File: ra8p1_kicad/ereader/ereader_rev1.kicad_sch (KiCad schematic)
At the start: 1 part, among them U1 R7KA8P1KFLCAC#UC0

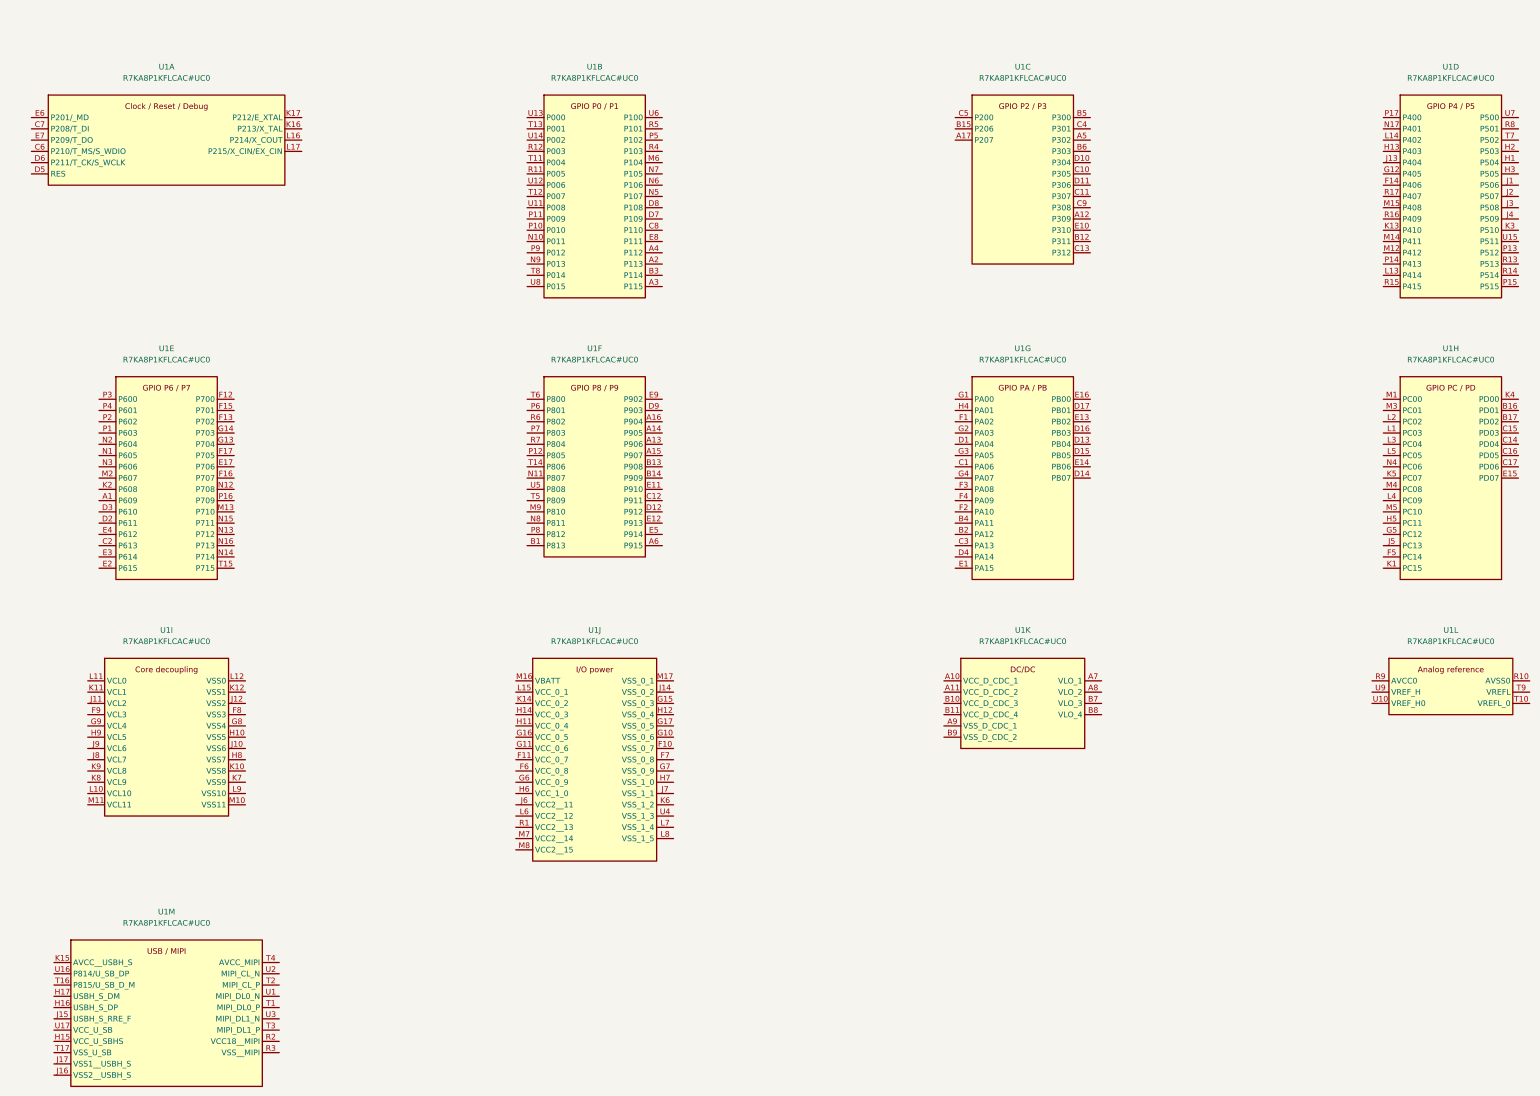
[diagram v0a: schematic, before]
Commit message: feat(hardware): split processor sheets and wire core power draft
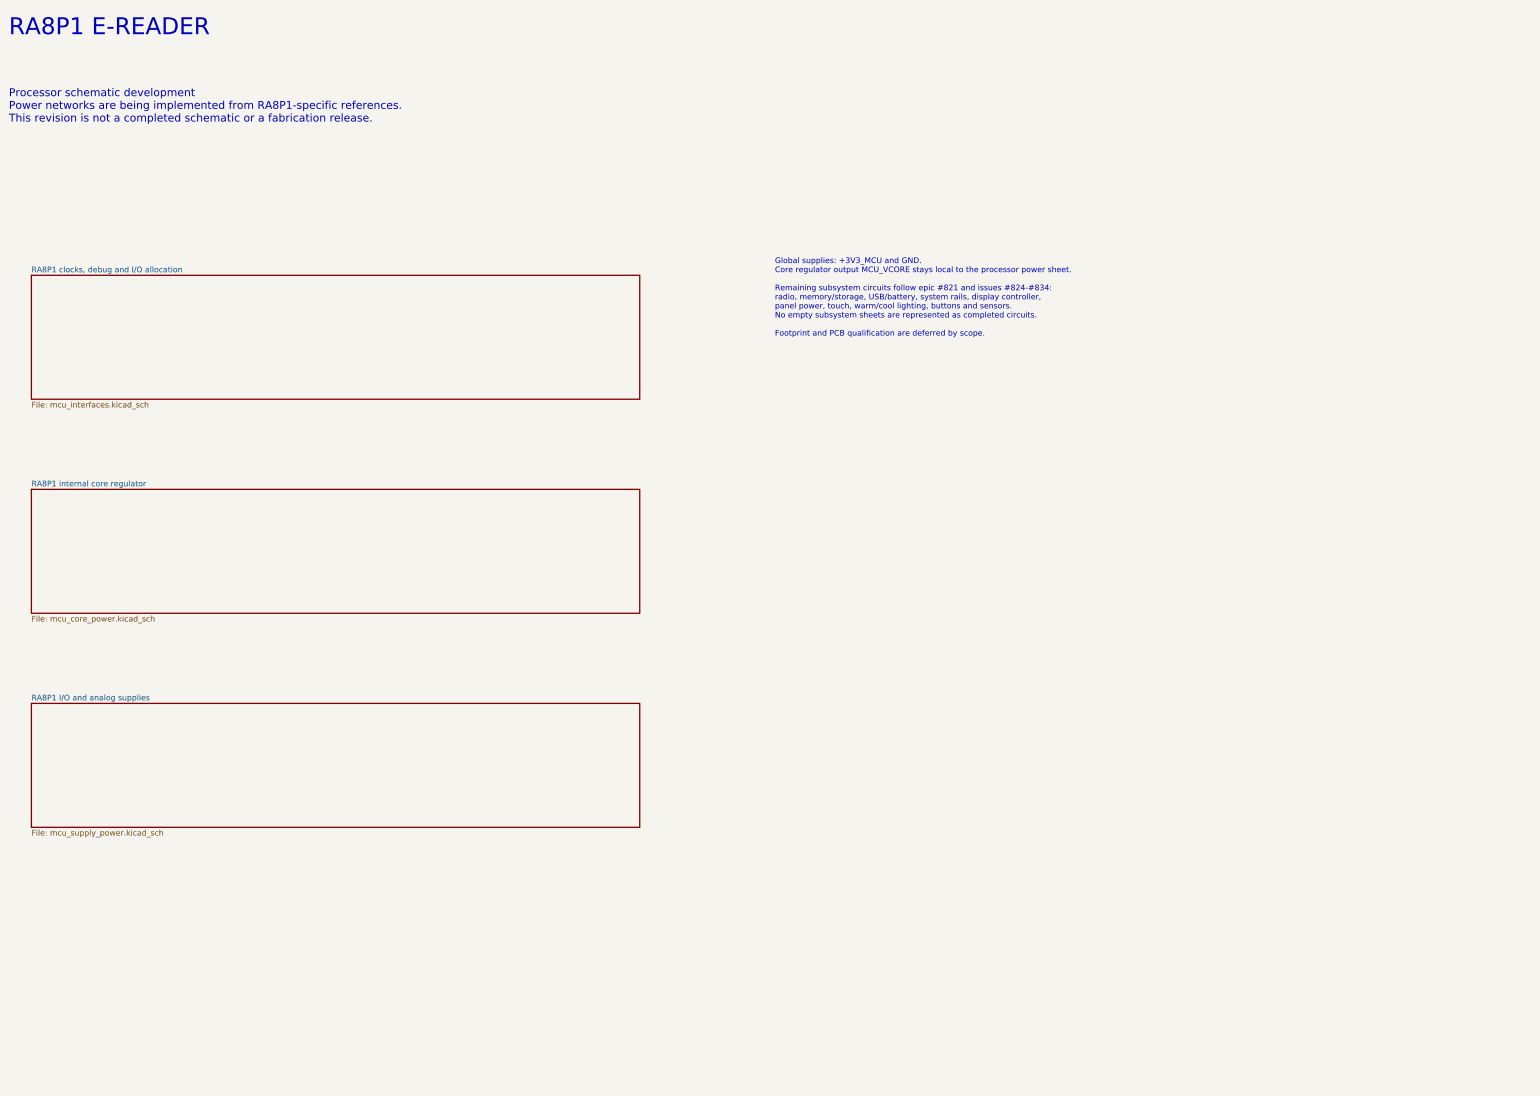
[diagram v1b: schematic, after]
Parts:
- removed U1: R7KA8P1KFLCAC#UC0, Processors:BGA289C65P17X17_1200X1200X138, symbol Processors:R7KA8P1KFLCAC#UC0
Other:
- added sheet RA8P1 I/O and analog supplies (mcu_supply_power.kicad_sch)
- added sheet RA8P1 clocks, debug and I/O allocation (mcu_interfaces.kicad_sch)
- added sheet RA8P1 internal core regulator (mcu_core_power.kicad_sch)
- note added: "Global supplies: +3V3_MCU and GND. Core regulator output MCU_VCORE stays local to the processor power sheet. Remaining subsystem circuits follow epic #821 and issues #824-#834: radio, memory/storage, USB/battery, system rails, display controller, panel power, touch, warm/cool lighting, buttons and sensors. No empty subsystem sheets are represented as completed circuits. Footprint and PCB qualific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"
- note added: "Processor schematic development Power networks are being implemented from RA8P1-specific references. This revision is not a completed schematic or a fabrication release."
- note added: "RA8P1 E-READER"
- title: (none) -> RA8P1 e-reader - schematic index

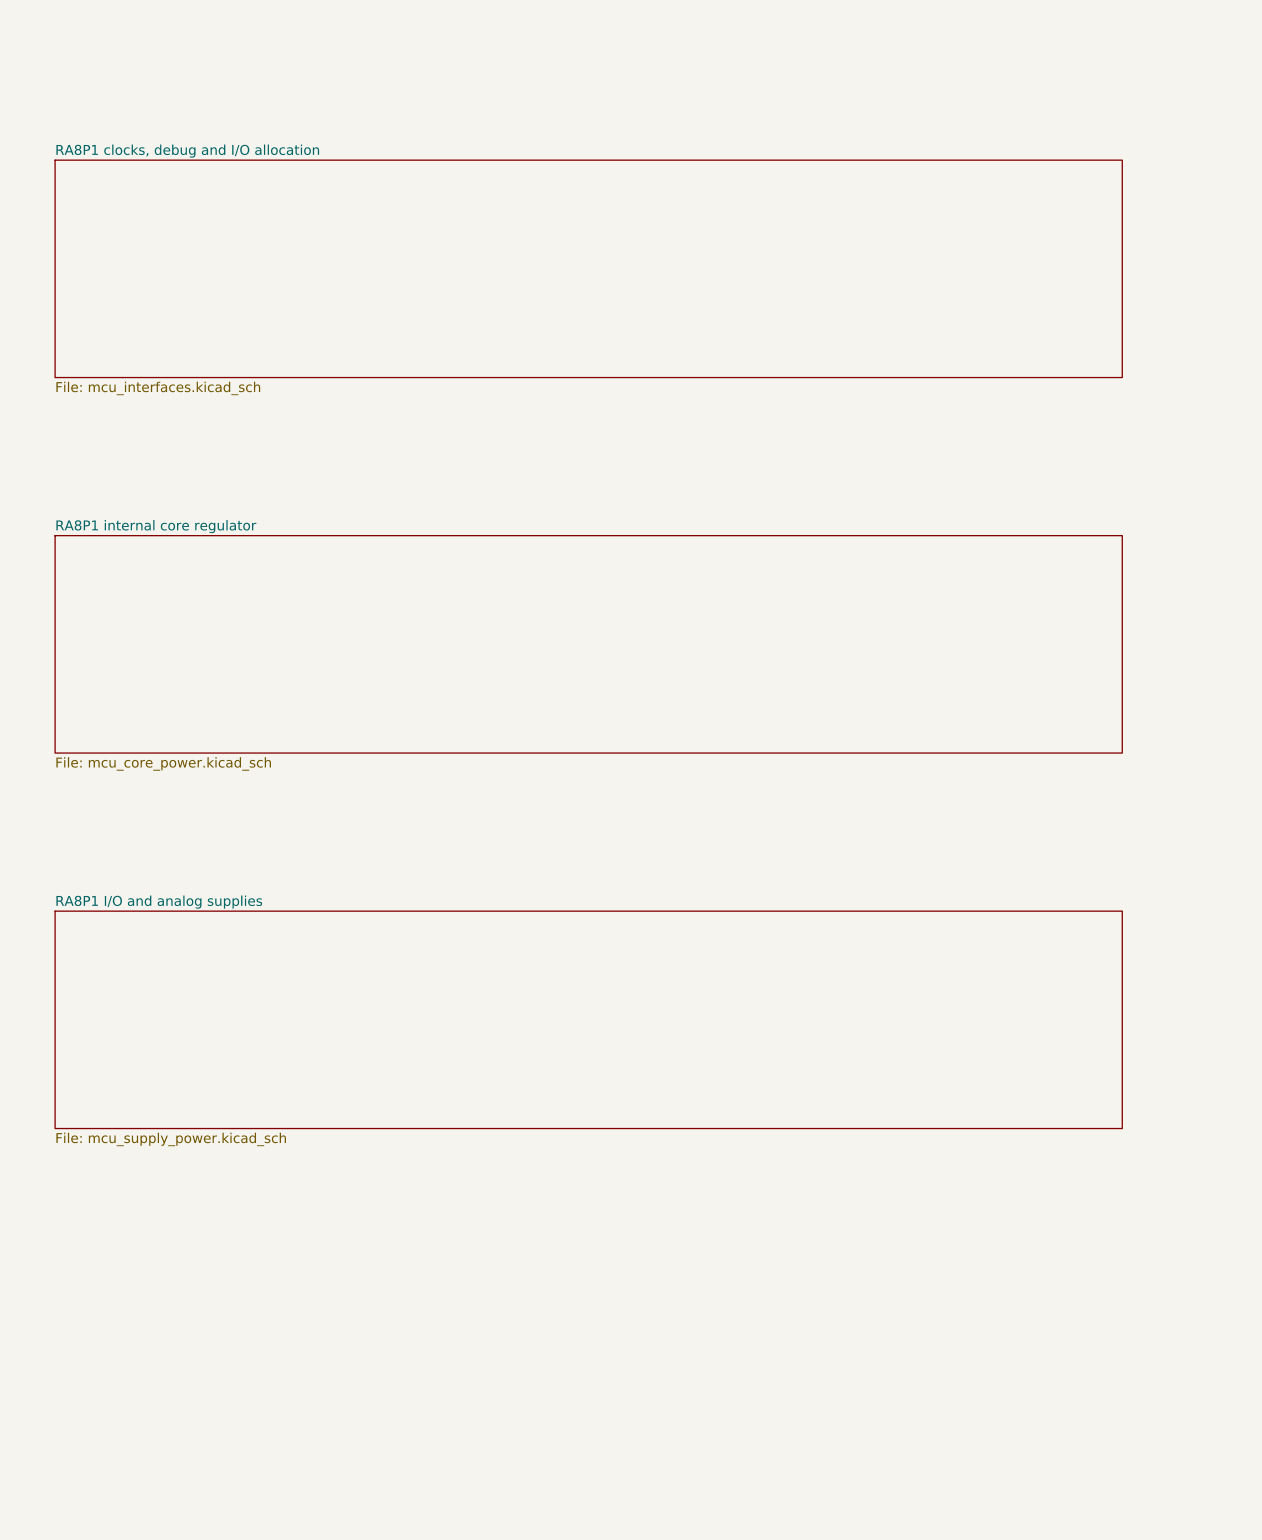
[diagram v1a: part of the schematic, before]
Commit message: feat(hardware): add RA8P1 boot debug draft and refine schematic presentation
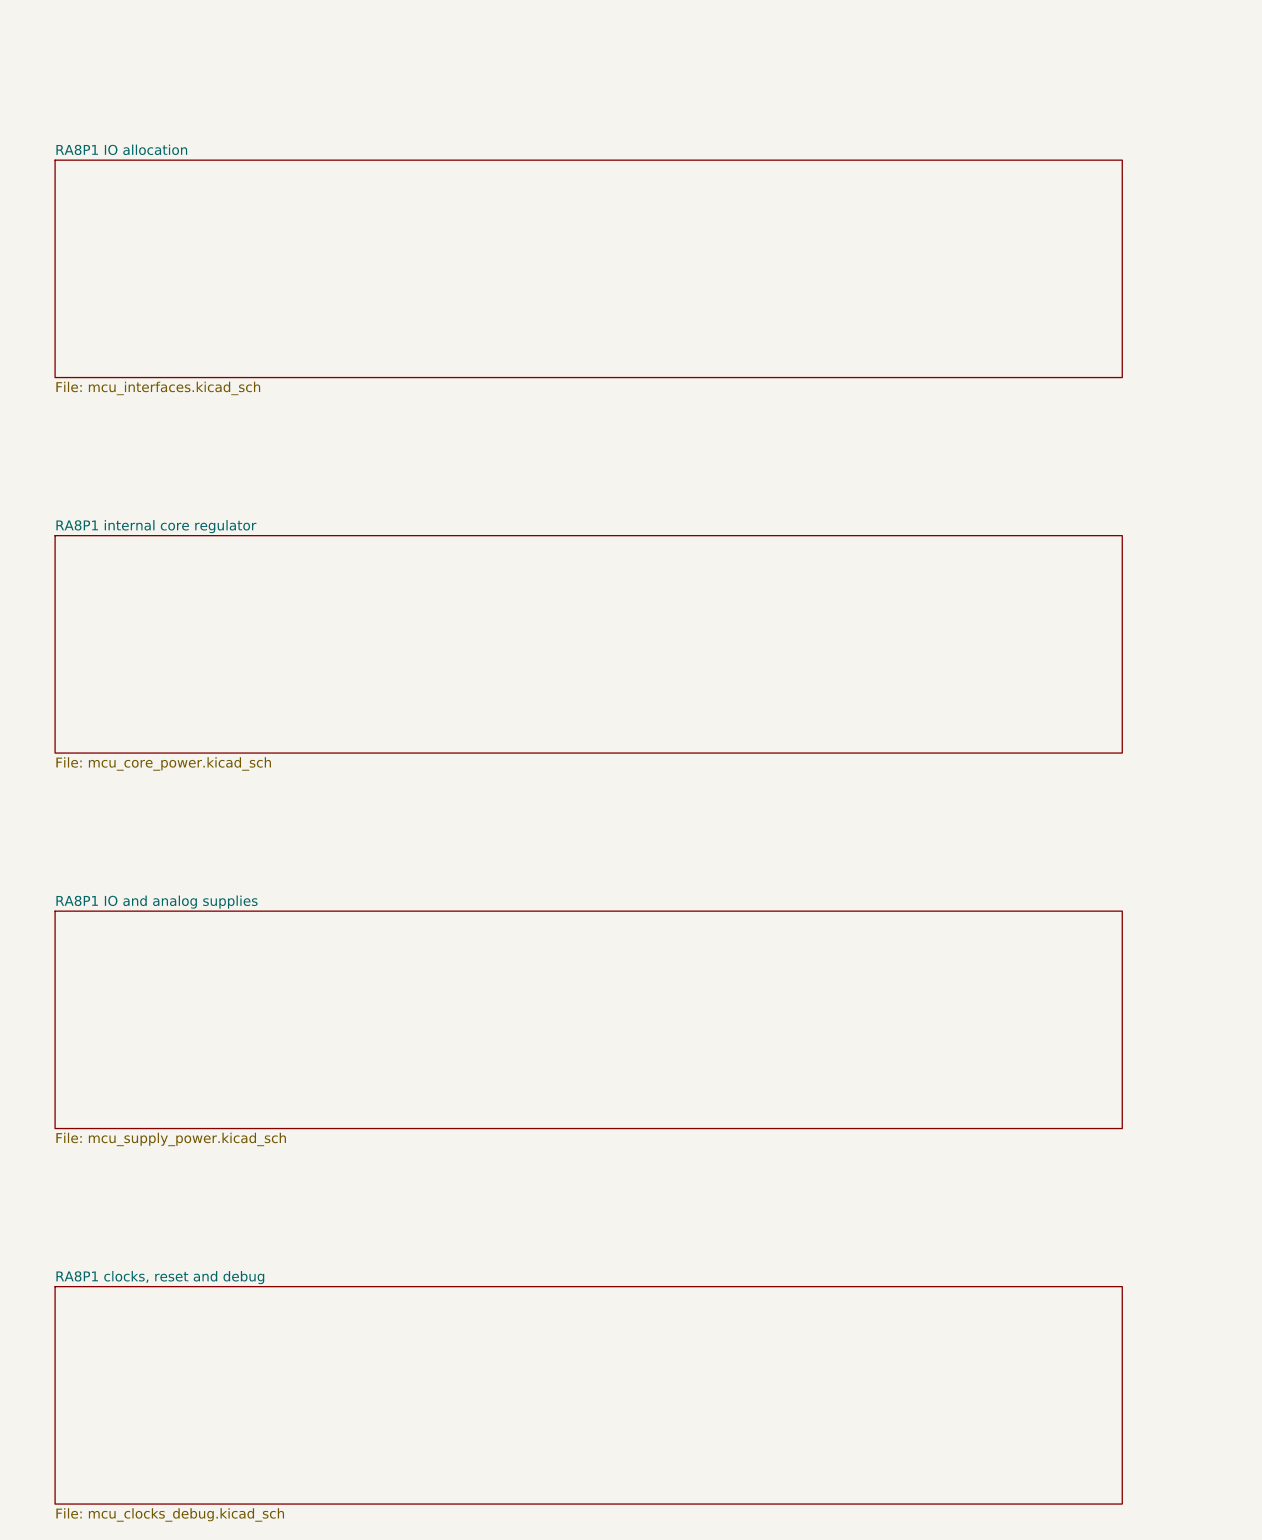
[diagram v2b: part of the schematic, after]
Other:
- sheet RA8P1 I/O and analog supplies renamed RA8P1 IO and analog supplies
- sheet RA8P1 clocks, debug and I/O allocation renamed RA8P1 IO allocation
- added sheet RA8P1 clocks, reset and debug (mcu_clocks_debug.kicad_sch)
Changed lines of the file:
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@@
 	(generator_version "10.0")
 	(paper "A3")
-	(sheet_instances
-		(path "/"
-			(page "1")
-		)
-	)
-	(embedded_fonts no)
 	(title_block
 		(title "RA8P1 e-reader - schematic index")
 		(date "2026-09-05")
-		(rev "0.2 DRAFT")
+		(rev "0.3 DRAFT")
 	)
 	(text "RA8P1 E-READER"
+		(exclude_from_sim no)
 		(at 25.4 25.4 0)
 		(effects
@@
 		)
 	)
+	(text "Global supplies: +3V3_MCU and GND.\nCore regulator output MCU_VCORE stays local to the processor power sheet.\n\nRemaining subsystem circuits follow epic #821 and issues #824-#834:\nradio, memory/storage, USB/battery, system rails, display controller,\npanel power, touch, warm/cool lighting, buttons and sensors.\nNo empty subsystem sheets are represented as completed circuits.\n\nFootprint and PCB qualification are deferred by scope."
+		(exclude_from_sim no)
+		(at 198.12 86.36 0)
+		(effects
+			(font
+				(size 1.27 1.27)
+			)
+			(justify left)
+		)
+	)
 	(text "Processor schematic development\nPower networks are being implemented from RA8P1-specific references.\nThis revision is not a completed schematic or a fabrication release."
+		(exclude_from_sim no)
 		(at 25.4 43.18 0)
 		(effects
@@
 	)
 	(sheet
+		(at 30.48 226.06)
+		(size 137.16 27.94)
+		(exclude_from_sim no)
+		(in_bom yes)
+		(on_board yes)
+		(dnp no)
+		(stroke
+			(width 0)
+			(type solid)
+		)
+		(fill
+			(color 0 0 0 0)
+		)
+		(property "Sheetname" "RA8P1 clocks, reset and debug"
+			(at 30.48 224.79 0)
+			(show_name no)
+			(do_not_autoplace no)
+			(effects
+				(font
+					(size 1.27 1.27)
+				)
+				(justify left)
+			)
+		)
+		(property "Sheetfile" "mcu_clocks_debug.kicad_sch"
+			(at 30.48 255.27 0)
+			(show_name no)
+			(do_not_autoplace no)
+			(effects
+				(font
+					(size 1.27 1.27)
+				)
+				(justify left)
+			)
+		)
+		(instances
+			(project "ereader_rev1"
+				(path "/0586cc51-9c57-495b-a0c9-c29ba0d48166"
+					(page "5")
+				)
+			)
+		)
+	)
+	(sheet
 		(at 30.48 81.28)
 		(size 137.16 27.94)
-		(stroke
-			(width 0)
-			(type default)
-		)
-		(fill
-			(color 0 0 0 0)
-		)
-		(property "Sheetname" "RA8P1 clocks, debug and I/O allocation"
+		(exclude_from_sim no)
+		(in_bom yes)
+		(on_board yes)
+		(dnp no)
+		(stroke
+			(width 0)
+			(type solid)
+		)
+		(fill
+			(color 0 0 0 0)
+		)
+		(property "Sheetname" "RA8P1 IO allocation"
 			(at 30.48 80.01 0)
+			(show_name no)
+			(do_not_autoplace no)
 			(effects
 				(font
@@
 		(property "Sheetfile" "mcu_interfaces.kicad_sch"
 			(at 30.48 110.49 0)
+			(show_name no)
+			(do_not_autoplace no)
 			(effects
 				(font
@@
 		(at 30.48 129.54)
 		(size 137.16 27.94)
-		(stroke
-			(width 0)
-			(type default)
+		(exclude_from_sim no)
+		(in_bom yes)
+		(on_board yes)
+		(dnp no)
+		(stroke
+			(width 0)
+			(type solid)
 		)
 		(fill
@@
 		(property "Sheetname" "RA8P1 internal core regulator"
 			(at 30.48 128.27 0)
+			(show_name no)
+			(do_not_autoplace no)
 			(effects
 				(font
@@
 		(property "Sheetfile" "mcu_core_power.kicad_sch"
 			(at 30.48 158.75 0)
+			(show_name no)
+			(do_not_autoplace no)
 			(effects
 				(font
@@
 		(at 30.48 177.8)
 		(size 137.16 27.94)
-		(stroke
-			(width 0)
-			(type default)
-		)
-		(fill
-			(color 0 0 0 0)
-		)
-		(property "Sheetname" "RA8P1 I/O and analog supplies"
+		(exclude_from_sim no)
+		(in_bom yes)
+		(on_board yes)
+		(dnp no)
+		(stroke
+			(width 0)
+			(type solid)
+		)
+		(fill
+			(color 0 0 0 0)
+		)
+		(property "Sheetname" "RA8P1 IO and analog supplies"
 			(at 30.48 176.53 0)
+			(show_name no)
+			(do_not_autoplace no)
 			(effects
 				(font
@@
 		(property "Sheetfile" "mcu_supply_power.kicad_sch"
 			(at 30.48 207.01 0)
+			(show_name no)
+			(do_not_autoplace no)
 			(effects
 				(font
@@
 		)
 	)
-	(text "Global supplies: +3V3_MCU and GND.\nCore regulator output MCU_VCORE stays local to the processor power sheet.\n\nRemaining subsystem circuits follow epic #821 and issues #824-#834:\nradio, memory/storage, USB/battery, system rails, display controller,\npanel power, touch, warm/cool lighting, buttons and sensors.\nNo empty subsystem sheets are represented as completed circuits.\n\nFootprint and PCB qualification are deferred by scope."
-		(at 198.12 86.36 0)
-		(effects
-			(font
-				(size 1.27 1.27)
-			)
-			(justify left)
-		)
-	)
+	(sheet_instances
+		(path "/"
+			(page "1")
+		)
+	)
+	(embedded_fonts no)
 )
